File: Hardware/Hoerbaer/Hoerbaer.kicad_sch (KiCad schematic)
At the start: 40 parts, among them J1 I2C, J13 JTAG, J17 RST_BOOT, J2 DISPLAY, J3 Micro_SD_Card_Det1, J4 USB1, J5 ENCODER, SW1 RESET, SW2 PROG, U1 ESP32 S3 MINI

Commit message: Many small corrections, changed connectors, ...
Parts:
- J1, J17, J2, J5: now not fitted
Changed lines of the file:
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@@
   )
   (symbol (lib_id "Connector_Generic:Conn_01x07") (at 82.55 33.02 180) (unit 1)
-    (in_bom yes) (on_board yes) (dnp no)
+    (in_bom yes) (on_board yes) (dnp yes)
     (property "Reference" "J2" (at 80.01 34.29 0)
       (effects (font (size 1.27 1.27)) (justify left))
@@
   )
   (symbol (lib_id "Connector_Generic:Conn_01x04") (at 273.05 151.13 0) (mirror x) (unit 1)
-    (in_bom yes) (on_board yes) (dnp no)
+    (in_bom yes) (on_board yes) (dnp yes)
     (property "Reference" "J5" (at 271.78 143.51 0)
       (effects (font (size 1.27 1.27)) (justify left))
@@
   )
   (symbol (lib_id "Connector_Generic:Conn_01x03") (at 214.63 52.07 0) (unit 1)
-    (in_bom yes) (on_board yes) (dnp no)
+    (in_bom yes) (on_board yes) (dnp yes)
     (property "Reference" "J17" (at 217.17 50.8 0)
       (effects (font (size 1.27 1.27)) (justify left))
@@
   )
   (symbol (lib_id "Connector_Generic:Conn_01x04") (at 30.48 33.02 180) (unit 1)
-    (in_bom yes) (on_board yes) (dnp no)
+    (in_bom yes) (on_board yes) (dnp yes)
     (property "Reference" "J1" (at 27.94 34.29 0)
       (effects (font (size 1.27 1.27)) (justify left))

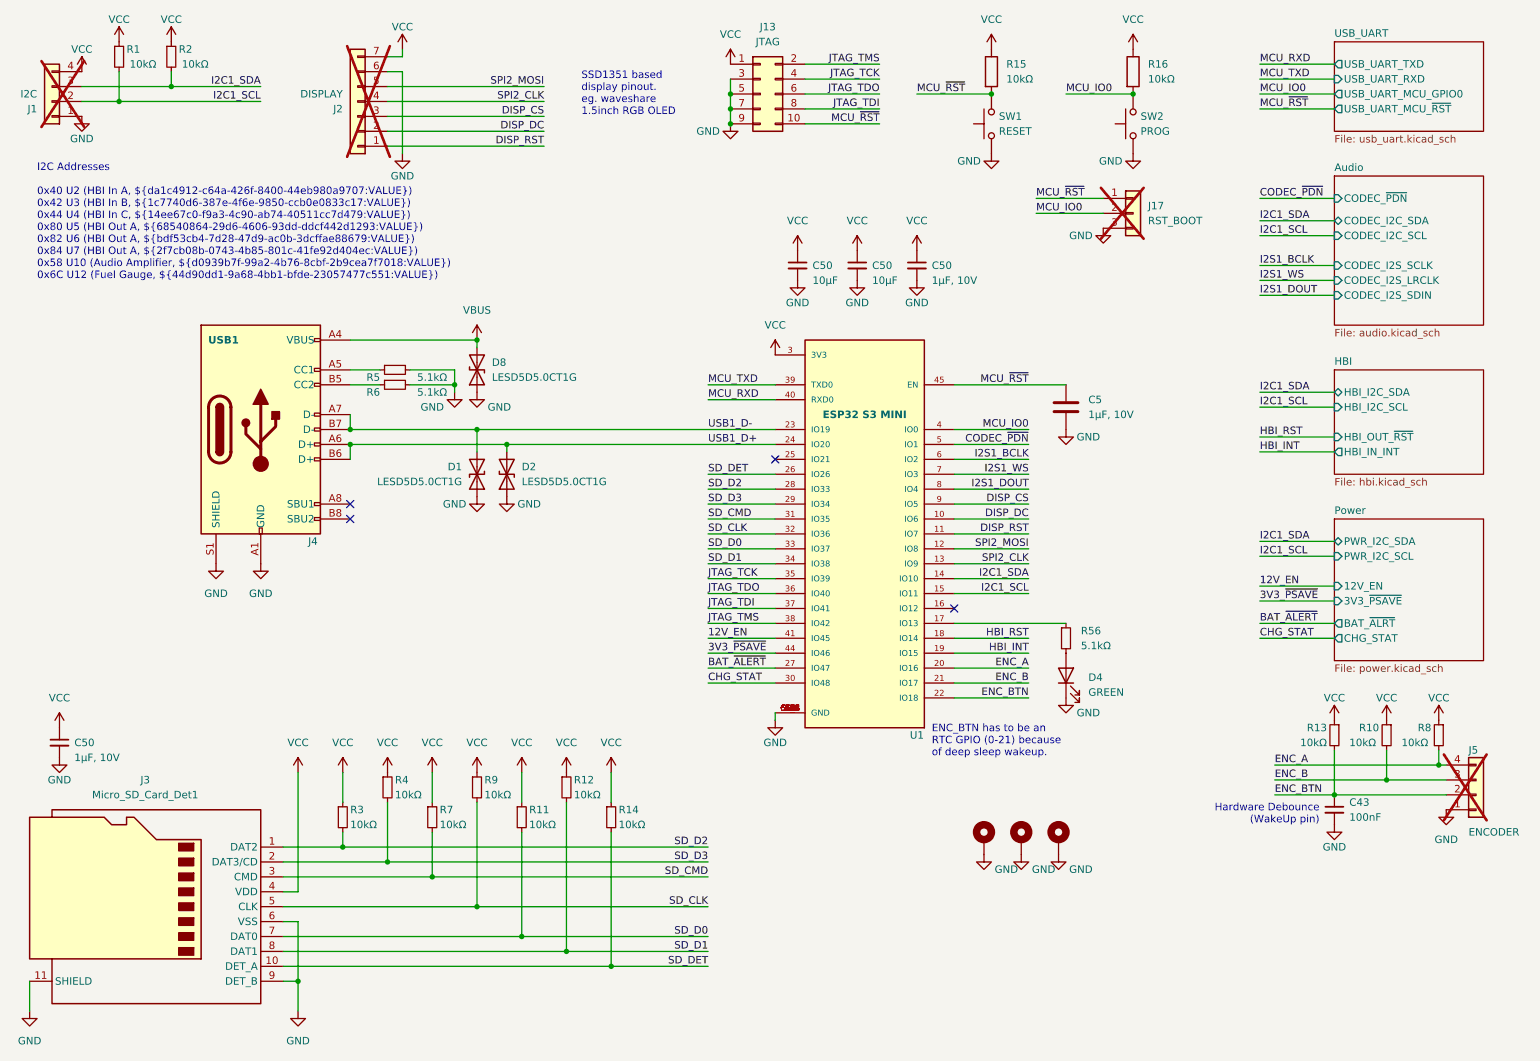
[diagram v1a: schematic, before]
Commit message: Added an additional connector. And silk screen designs.
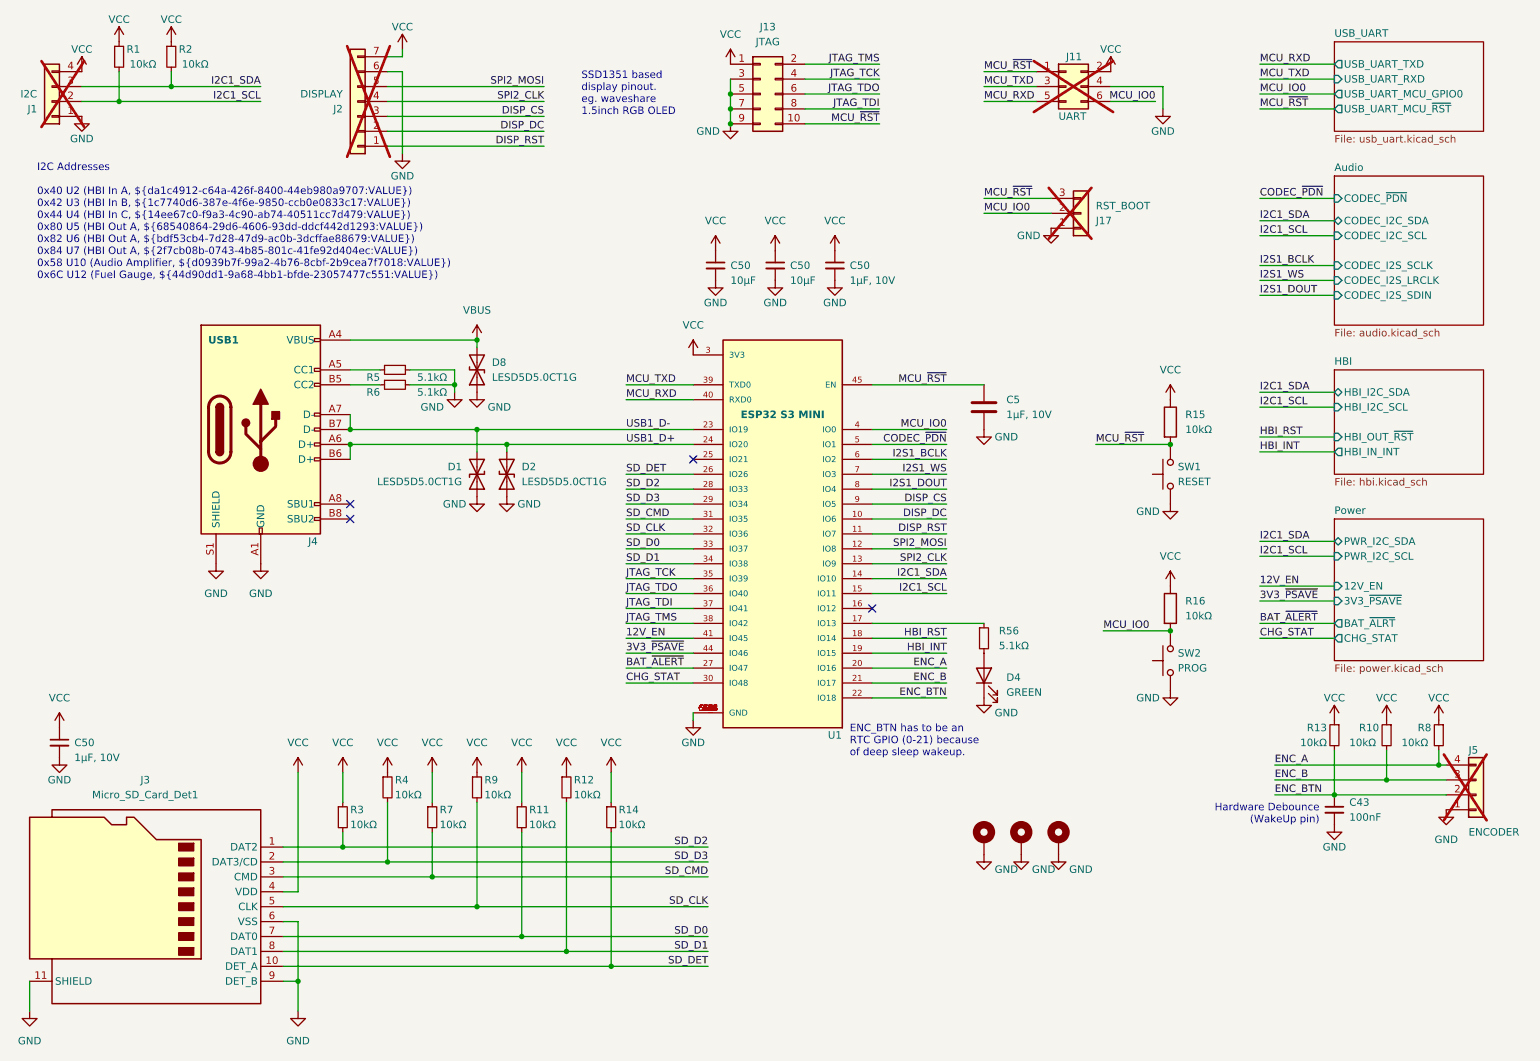
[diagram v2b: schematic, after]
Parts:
- added J11: UART, Connector_PinHeader_2.54mm:PinHeader_2x03_P2.54mm_Vertical, symbol Connector_Generic:Conn_02x03_Odd_Even
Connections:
- net GND: now also J17.1 (Pin_1), J11.4 (Pin_4); no longer J17.3 (Pin_3)
- net MCU_IO0: now also J11.6 (Pin_6)
- net MCU_RXD: now also J11.5 (Pin_5)
- net MCU_TXD: now also J11.3 (Pin_3)
- net MCU_~{RST}: now also J17.3 (Pin_3), J11.1 (Pin_1); no longer J17.1 (Pin_1)
- net VCC: now also J11.2 (Pin_2)
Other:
- moved on the sheet: C5, C50, D4, J17, R15, R16, R56, SW1, SW2, U1

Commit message: Fixed 1uF order number.
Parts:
- C5, C50: LCSC C726581 -> C29266; MPN AC0805KKX7R6BB105 -> CL05A105KO5NNNC
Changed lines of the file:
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@@
       (effects (font (size 1.27 1.27)) hide)
     )
-    (property "LCSC" "C726581" (at 189.23 85.09 0)
-      (effects (font (size 1.27 1.27)) hide)
-    )
-    (property "MPN" "AC0805KKX7R6BB105" (at 189.23 85.09 0)
+    (property "LCSC" "C29266 " (at 189.23 85.09 0)
+      (effects (font (size 1.27 1.27)) hide)
+    )
+    (property "MPN" "CL05A105KO5NNNC" (at 189.23 85.09 0)
       (effects (font (size 1.27 1.27)) hide)
     )
@@
       (effects (font (size 1.27 1.27)) hide)
     )
-    (property "LCSC" "C726581" (at 31.75 142.24 0)
-      (effects (font (size 1.27 1.27)) hide)
-    )
-    (property "MPN" "AC0805KKX7R6BB105" (at 31.75 142.24 0)
+    (property "LCSC" "C29266 " (at 31.75 142.24 0)
+      (effects (font (size 1.27 1.27)) hide)
+    )
+    (property "MPN" "CL05A105KO5NNNC" (at 31.75 142.24 0)
       (effects (font (size 1.27 1.27)) hide)
     )
@@
       (effects (font (size 1.27 1.27)) hide)
     )
-    (property "LCSC" "C726581" (at 163.83 60.96 0)
-      (effects (font (size 1.27 1.27)) hide)
-    )
-    (property "MPN" "AC0805KKX7R6BB105" (at 163.83 60.96 0)
-      (effects (font (size 1.27 1.27)) hide)
-    )
+    (property "LCSC" "C29266 " (at 163.83 60.96 0)
+      (effects (font (size 1.27 1.27)) hide)
+    )
+    (property "MPN" "CL05A105KO5NNNC" (at 163.83 60.96 0)
+      (effects (font (size 1.27 1.27)) hide)
+    )

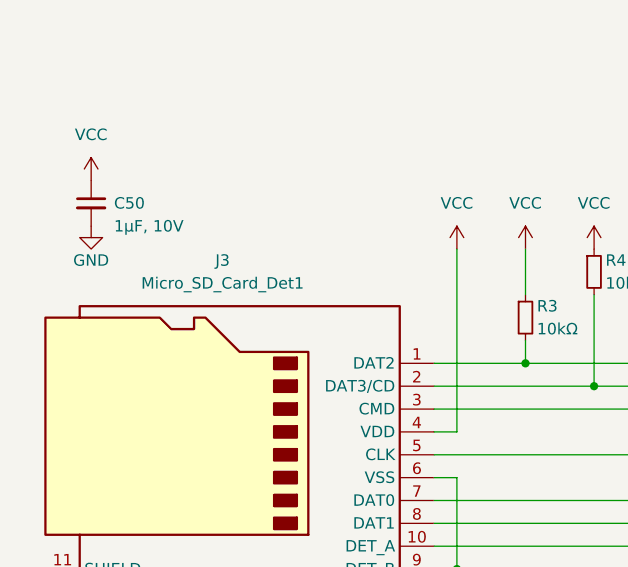
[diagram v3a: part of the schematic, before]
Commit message: Added sd card reverse adapter pcb
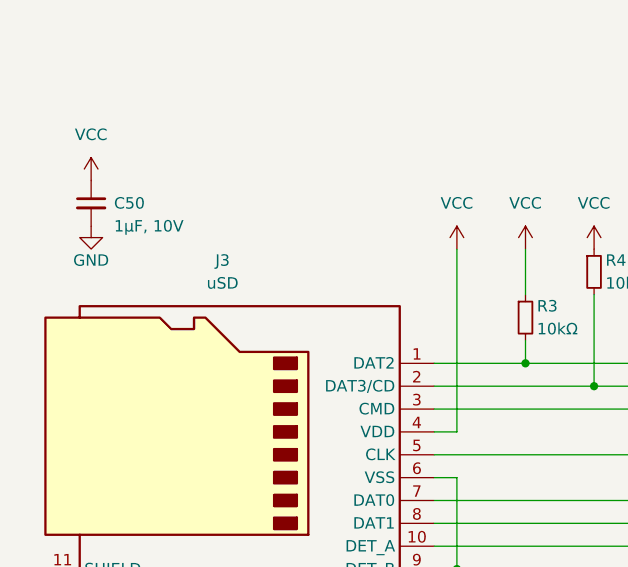
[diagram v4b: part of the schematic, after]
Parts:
- J3: value Micro_SD_Card_Det1 -> uSD
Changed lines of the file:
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@@
       (effects (font (size 1.27 1.27)))
     )
-    (property "Value" "Micro_SD_Card_Det1" (at 46.355 151.13 0)
+    (property "Value" "uSD" (at 46.355 151.13 0)
       (effects (font (size 1.27 1.27)))
     )

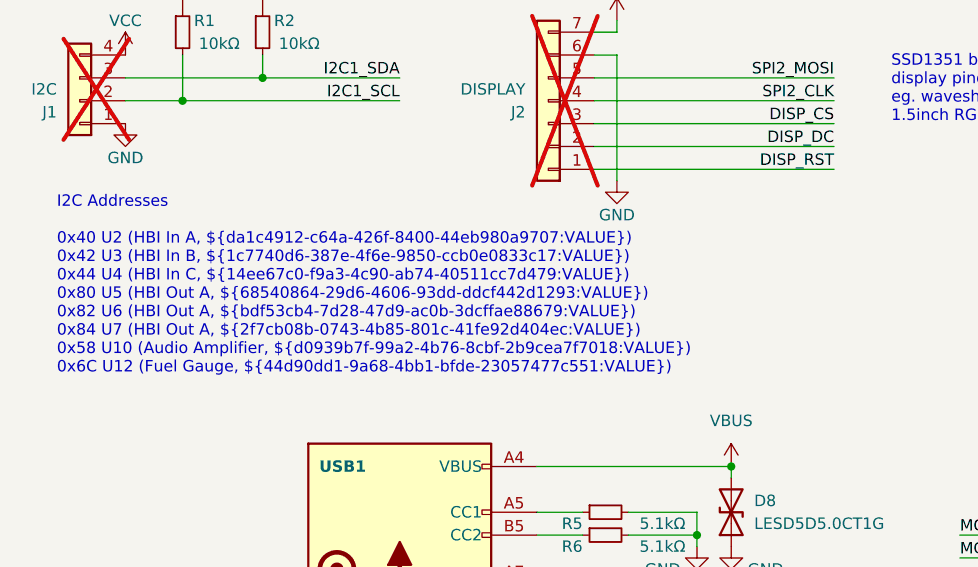
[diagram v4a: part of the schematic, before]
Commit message: Fixed I2C addresses
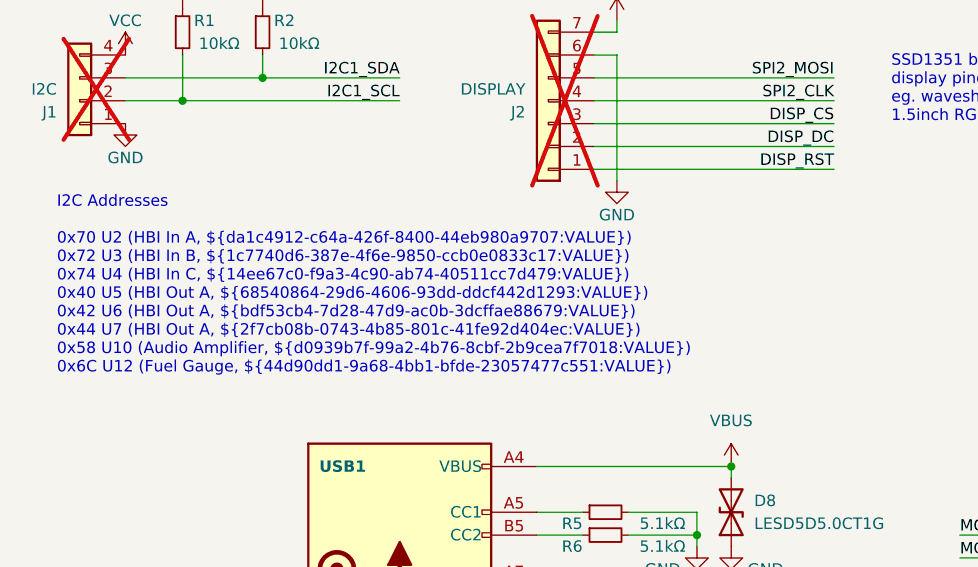
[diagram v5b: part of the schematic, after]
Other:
- note added: "I2C Addresses 0x70 U2 (HBI In A, ${da1c4912-c64a-426f-8400-44eb980a9707:VALUE}) 0x72 U3 (HBI In B, ${1c7740d6-387e-4f6e-9850-ccb0e0833c17:VALUE}) 0x74 U4 (HBI In C, ${14ee67c0-f9a3-4c90-ab74-40511cc7d479:VALUE}) 0x40 U5 (HBI Out A, ${68540864-29d6-4606-93dd-ddcf442d1293:VALUE}) 0x42 U6 (HBI Out A, ${bdf53cb4-7d28-47d9-ac0b-3dcffae88679:VALUE}) 0x44 U7 (HBI Out A, ${2f7cb08b-0743-4b85-801c-41fe92d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"
- note removed: "I2C Addresses 0x40 U2 (HBI In A, ${da1c4912-c64a-426f-8400-44eb980a9707:VALUE}) 0x42 U3 (HBI In B, ${1c7740d6-387e-4f6e-9850-ccb0e0833c17:VALUE}) 0x44 U4 (HBI In C, ${14ee67c0-f9a3-4c90-ab74-40511cc7d479:VALUE}) 0x80 U5 (HBI Out A, ${68540864-29d6-4606-93dd-ddcf442d1293:VALUE}) 0x82 U6 (HBI Out A, ${bdf53cb4-7d28-47d9-ac0b-3dcffae88679:VALUE}) 0x84 U7 (HBI Out A, ${2f7cb08b-0743-4b85-801c-41fe92d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"
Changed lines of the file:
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@@
     (effects (font (size 1.27 1.27)) (justify left bottom))
   )
-  (text "I2C Addresses\n\n0x40 U2 (HBI In A, ${da1c4912-c64a-426f-8400-44eb980a9707:VALUE})\n0x42 U3 (HBI In B, ${1c7740d6-387e-4f6e-9850-ccb0e0833c17:VALUE})\n0x44 U4 (HBI In C, ${14ee67c0-f9a3-4c90-ab74-40511cc7d479:VALUE})\n0x80 U5 (HBI Out A, ${68540864-29d6-4606-93dd-ddcf442d1293:VALUE})\n0x82 U6 (HBI Out A, ${bdf53cb4-7d28-47d9-ac0b-3dcffae88679:VALUE})\n0x84 U7 (HBI Out A, ${2f7cb08b-0743-4b85-801c-41fe92d404ec:VALUE})\n0x58 U10 (Audio Amplifier, ${d0939b7f-99a2-4b76-8cbf-2b9cea7f7018:VALUE})\n0x6C U12 (Fuel Gauge, ${44d90dd1-9a68-4bb1-bfde-23057477c551:VALUE})"
+  (text "I2C Addresses\n\n0x70 U2 (HBI In A, ${da1c4912-c64a-426f-8400-44eb980a9707:VALUE})\n0x72 U3 (HBI In B, ${1c7740d6-387e-4f6e-9850-ccb0e0833c17:VALUE})\n0x74 U4 (HBI In C, ${14ee67c0-f9a3-4c90-ab74-40511cc7d479:VALUE})\n0x40 U5 (HBI Out A, ${68540864-29d6-4606-93dd-ddcf442d1293:VALUE})\n0x42 U6 (HBI Out A, ${bdf53cb4-7d28-47d9-ac0b-3dcffae88679:VALUE})\n0x44 U7 (HBI Out A, ${2f7cb08b-0743-4b85-801c-41fe92d404ec:VALUE})\n0x58 U10 (Audio Amplifier, ${d0939b7f-99a2-4b76-8cbf-2b9cea7f7018:VALUE})\n0x6C U12 (Fuel Gauge, ${44d90dd1-9a68-4bb1-bfde-23057477c551:VALUE})"
     (at 27.94 63.5 0)
     (effects (font (size 1.27 1.27)) (justify left bottom))

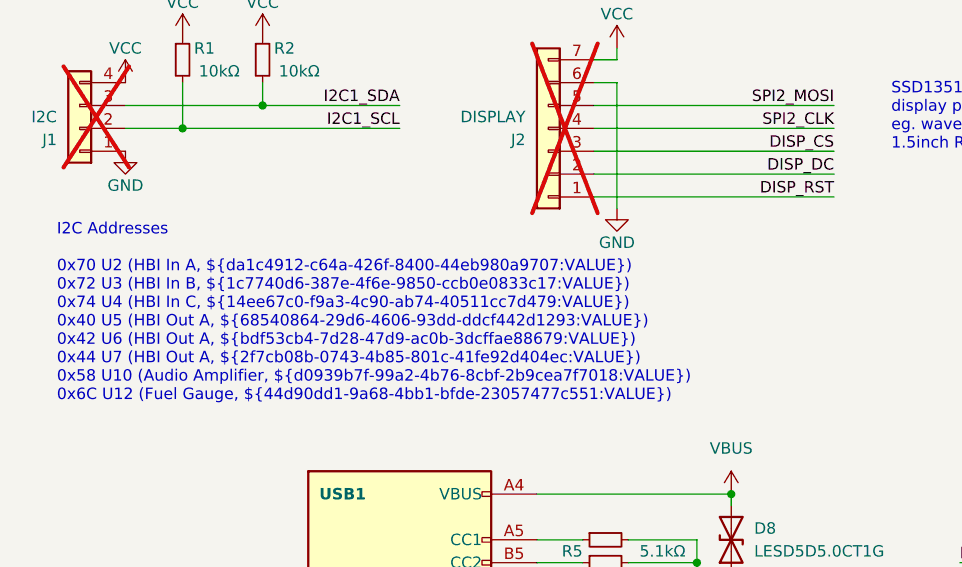
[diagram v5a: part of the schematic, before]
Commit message: Setup input expanders
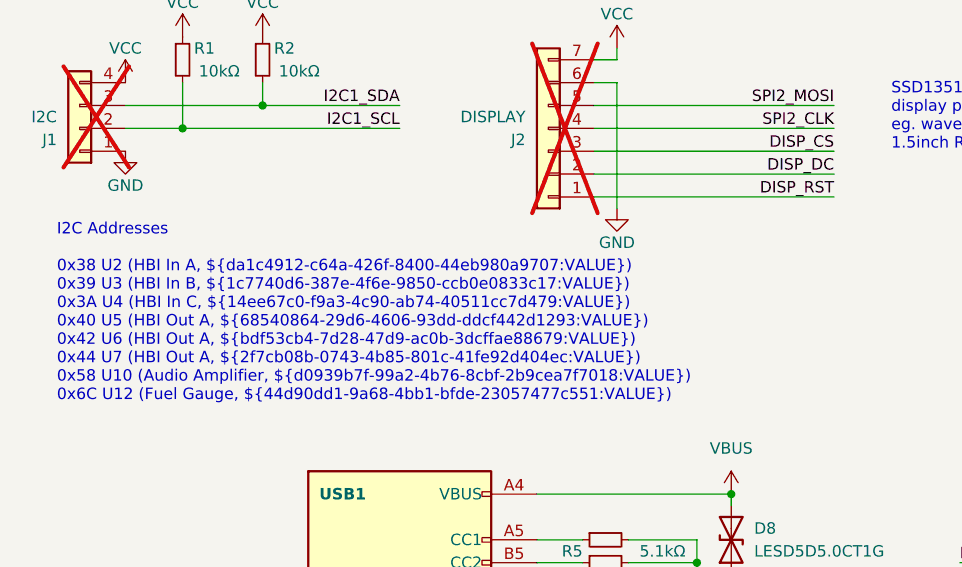
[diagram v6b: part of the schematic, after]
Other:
- note added: "I2C Addresses 0x38 U2 (HBI In A, ${da1c4912-c64a-426f-8400-44eb980a9707:VALUE}) 0x39 U3 (HBI In B, ${1c7740d6-387e-4f6e-9850-ccb0e0833c17:VALUE}) 0x3A U4 (HBI In C, ${14ee67c0-f9a3-4c90-ab74-40511cc7d479:VALUE}) 0x40 U5 (HBI Out A, ${68540864-29d6-4606-93dd-ddcf442d1293:VALUE}) 0x42 U6 (HBI Out A, ${bdf53cb4-7d28-47d9-ac0b-3dcffae88679:VALUE}) 0x44 U7 (HBI Out A, ${2f7cb08b-0743-4b85-801c-41fe92d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"
- note removed: "I2C Addresses 0x70 U2 (HBI In A, ${da1c4912-c64a-426f-8400-44eb980a9707:VALUE}) 0x72 U3 (HBI In B, ${1c7740d6-387e-4f6e-9850-ccb0e0833c17:VALUE}) 0x74 U4 (HBI In C, ${14ee67c0-f9a3-4c90-ab74-40511cc7d479:VALUE}) 0x40 U5 (HBI Out A, ${68540864-29d6-4606-93dd-ddcf442d1293:VALUE}) 0x42 U6 (HBI Out A, ${bdf53cb4-7d28-47d9-ac0b-3dcffae88679:VALUE}) 0x44 U7 (HBI Out A, ${2f7cb08b-0743-4b85-801c-41fe92d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"
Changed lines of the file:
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@@
     (effects (font (size 1.27 1.27)) (justify left bottom))
   )
-  (text "I2C Addresses\n\n0x70 U2 (HBI In A, ${da1c4912-c64a-426f-8400-44eb980a9707:VALUE})\n0x72 U3 (HBI In B, ${1c7740d6-387e-4f6e-9850-ccb0e0833c17:VALUE})\n0x74 U4 (HBI In C, ${14ee67c0-f9a3-4c90-ab74-40511cc7d479:VALUE})\n0x40 U5 (HBI Out A, ${68540864-29d6-4606-93dd-ddcf442d1293:VALUE})\n0x42 U6 (HBI Out A, ${bdf53cb4-7d28-47d9-ac0b-3dcffae88679:VALUE})\n0x44 U7 (HBI Out A, ${2f7cb08b-0743-4b85-801c-41fe92d404ec:VALUE})\n0x58 U10 (Audio Amplifier, ${d0939b7f-99a2-4b76-8cbf-2b9cea7f7018:VALUE})\n0x6C U12 (Fuel Gauge, ${44d90dd1-9a68-4bb1-bfde-23057477c551:VALUE})"
+  (text "I2C Addresses\n\n0x38 U2 (HBI In A, ${da1c4912-c64a-426f-8400-44eb980a9707:VALUE})\n0x39 U3 (HBI In B, ${1c7740d6-387e-4f6e-9850-ccb0e0833c17:VALUE})\n0x3A U4 (HBI In C, ${14ee67c0-f9a3-4c90-ab74-40511cc7d479:VALUE})\n0x40 U5 (HBI Out A, ${68540864-29d6-4606-93dd-ddcf442d1293:VALUE})\n0x42 U6 (HBI Out A, ${bdf53cb4-7d28-47d9-ac0b-3dcffae88679:VALUE})\n0x44 U7 (HBI Out A, ${2f7cb08b-0743-4b85-801c-41fe92d404ec:VALUE})\n0x58 U10 (Audio Amplifier, ${d0939b7f-99a2-4b76-8cbf-2b9cea7f7018:VALUE})\n0x6C U12 (Fuel Gauge, ${44d90dd1-9a68-4bb1-bfde-23057477c551:VALUE})"
     (at 27.94 63.5 0)
     (effects (font (size 1.27 1.27)) (justify left bottom))

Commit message: Added 3d model for USB footprint.
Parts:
- J4: footprint Connector_USB:USB_C_Receptacle_HRO_TYPE-C-31-M-12 -> Baer_Footprints:USB_C_Receptacle_HRO_TYPE-C-31-M-12
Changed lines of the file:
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@@
       (effects (font (size 1.27 1.27) bold))
     )
-    (property "Footprint" "Connector_USB:USB_C_Receptacle_HRO_TYPE-C-31-M-12" (at 69.85 88.9 0)
+    (property "Footprint" "Baer_Footprints:USB_C_Receptacle_HRO_TYPE-C-31-M-12" (at 69.85 88.9 0)
       (effects (font (size 1.27 1.27)) hide)
     )
